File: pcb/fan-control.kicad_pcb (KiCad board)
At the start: 2 copper layers, 30 x 65 mm, 47 parts, among them J1 USB_C_Receptacle_USB2.0_14P, J2 USB_C_Receptacle_USB2.0_14P, Q1 BSS138, SW1 SW_Push, SW2 SW_Push, U1 ESP32-C6-WROOM-1-N8, U2 MPM3610GQV-P

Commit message: some layout
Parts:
- D1, D10, D2, D3, D4, D5, D6, D7, D8, D9: moved to B.Cu
- SW1: footprint Button_Switch_THT:SW_PUSH_6mm -> Footprints:4P-3.4x3.4mm; moved to B.Cu
- SW2: footprint Button_Switch_THT:SW_PUSH_6mm -> Footprints:4P-3.4x3.4mm
- moved R1 80.1 mm to (161.8, 122.0), turned to 180 degrees
- moved R2 79.8 mm to (161.8, 113.1), turned to 180 degrees
- moved R5 77.5 mm to (147.9, 83.2)
- moved R18 76.9 mm to (154.3, 78.2), turned to 90 degrees
- moved R8 75.5 mm to (161.8, 110.6), turned to 180 degrees
- moved C1 73.7 mm to (154.2, 93.8), turned to 90 degrees
- moved R19 73.5 mm to (150.9, 81.7), turned to 90 degrees
- moved R4 70.3 mm to (145.1, 90.4), turned to 90 degrees
- moved R6 69.2 mm to (147.9, 77.3)
- moved R7 68.5 mm to (152.6, 93.8), turned to -90 degrees
- moved R23 67.7 mm to (151.5, 79.1)
- moved R22 67.2 mm to (151.5, 77.4), turned to 180 degrees
- moved R3 67.1 mm to (145.1, 95.9), turned to -90 degrees
- moved R20 63.5 mm to (152.5, 81.7), turned to -90 degrees
- moved C4 63.0 mm to (144.5, 103.5), turned to 90 degrees
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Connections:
- D1 pad 1: /LED1 -> Net-(D1-K)
- D1 pad 2: Net-(D1-A) -> +3V3
- D10 pad 1: /LED10 -> Net-(D10-K)
- D10 pad 2: Net-(D10-A) -> +3V3
- D2 pad 1: /LED2 -> Net-(D2-K)
- D2 pad 2: Net-(D2-A) -> +3V3
- D3 pad 1: /LED3 -> Net-(D3-K)
- D3 pad 2: Net-(D3-A) -> +3V3
- D4 pad 1: /LED4 -> Net-(D4-K)
- D4 pad 2: Net-(D4-A) -> +3V3
- D5 pad 1: /LED5 -> Net-(D5-K)
- D5 pad 2: Net-(D5-A) -> +3V3
- D6 pad 1: /LED6 -> Net-(D6-K)
- D6 pad 2: Net-(D6-A) -> +3V3
- D7 pad 1: /LED7 -> Net-(D7-K)
- D7 pad 2: Net-(D7-A) -> +3V3
- D8 pad 1: /LED8 -> Net-(D8-K)
- D8 pad 2: Net-(D8-A) -> +3V3
- D9 pad 1: /LED9 -> Net-(D9-K)
- D9 pad 2: Net-(D9-A) -> +3V3
- R10 pad 1: +3V3 -> Net-(D3-K)
- R10 pad 2: Net-(D3-A) -> /LED3
- R11 pad 1: +3V3 -> Net-(D4-K)
- R11 pad 2: Net-(D4-A) -> /LED4
- R12 pad 1: +3V3 -> Net-(D5-K)
- R12 pad 2: Net-(D5-A) -> /LED5
- R13 pad 1: +3V3 -> Net-(D6-K)
- R13 pad 2: Net-(D6-A) -> /LED6
- R14 pad 1: +3V3 -> Net-(D7-K)
- R14 pad 2: Net-(D7-A) -> /LED7
- R15 pad 1: +3V3 -> Net-(D8-K)
- R15 pad 2: Net-(D8-A) -> /LED8
- R16 pad 1: +3V3 -> Net-(D9-K)
- R16 pad 2: Net-(D9-A) -> /LED9
- R17 pad 1: +3V3 -> Net-(D10-K)
- R17 pad 2: Net-(D10-A) -> /LED10
- R8 pad 1: +3V3 -> Net-(D1-K)
- R8 pad 2: Net-(D1-A) -> /LED1
- R9 pad 1: +3V3 -> Net-(D2-K)
- R9 pad 2: Net-(D2-A) -> /LED2
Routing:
- net +10V: track 0.00 -> 23.4 mm, vias 0 -> 2
- net +3V3: track 0.00 -> 15.5 mm, vias 0 -> 2
- net /BOOT: track 0.00 -> 7.60 mm
- net /FAN_PWM: track 0.00 -> 6.65 mm
- net /BUTTON: track 0.00 -> 5.25 mm, vias 0 -> 1
- net Net-(J1-CC1): track 0.00 -> 4.47 mm
- net Net-(U2-FB): track 0.00 -> 3.70 mm
- net /LED5: track 0.00 -> 2.56 mm
- net /TACH: track 0.00 -> 2.46 mm
- net /D-: track 0.00 -> 2.44 mm
- net /D+: track 0.00 -> 2.44 mm
- net /LED6: track 0.00 -> 2.42 mm
- net /LED10: track 0.00 -> 2.40 mm
- net /LED3: track 0.00 -> 2.35 mm
- net /LED7: track 0.00 -> 2.29 mm
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
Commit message: Routing
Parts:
- removed J2: USB_C_Receptacle_USB2.0_14P, Connector_USB:USB_C_Receptacle_GCT_USB4105-xx-A_16P_TopMnt_Horizontal
- removed R3, R4: 5.1k, Resistor_SMD:R_0603_1608Metric_Pad0.98x0.95mm_HandSolder
- added J3: Conn_ARM_SWD_TagConnect_TC2030-NL, Connector:Tag-Connect_TC2030-IDC-NL_2x03_P1.27mm_Vertical, F.Cu at (137.6, 85.0)
- moved D3 35.6 mm to (158.8, 121.3)
- moved D4 35.6 mm to (158.8, 115.6)
- moved D1 35.6 mm to (150.0, 127.7)
- moved D10 35.6 mm to (144.6, 125.9)
- moved D2 35.6 mm to (155.4, 125.9)
- moved D5 35.6 mm to (155.4, 111.0)
- moved D6 35.6 mm to (150.0, 109.2)
- moved D7 35.6 mm to (144.6, 111.0)
- moved D8 35.6 mm to (141.2, 115.6)
- moved D9 35.6 mm to (141.2, 121.3)
- moved R1 34.6 mm to (152.7, 88.6), turned to -90 degrees
- moved R2 30.7 mm to (143.3, 88.6), turned to -90 degrees
- moved H1 27.2 mm to (150.0, 118.6)
- moved R16 25.0 mm to (137.4, 89.7)
- moved SW2 22.1 mm to (137.3, 124.1), turned to 90 degrees
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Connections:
- R10 pad 2: /LED3 -> /LED10
- R11 pad 2: /LED4 -> /LED1
- R12 pad 2: /LED5 -> /LED3
- R13 pad 2: /LED6 -> /LED2
- R14 pad 2: /LED7 -> /LED8
- R15 pad 2: /LED8 -> /LED5
- R16 pad 2: /LED9 -> /LED4
- R17 pad 2: /LED10 -> /LED6
- R8 pad 2: /LED1 -> /LED7
- R9 pad 2: /LED2 -> /LED9
- U1 pad 12: /LED1 -> unconnected-(U1-IO11-Pad12)
- U1 pad 13: /D- -> unconnected-(U1-IO12-Pad13)
- U1 pad 14: /D+ -> /LED4
- U1 pad 24: /LED4 -> /RX
- U1 pad 25: /LED3 -> /TX
- U1 pad 26: unconnected-(U1-IO3-Pad26) -> /LED1
- U1 pad 27: unconnected-(U1-IO2-Pad27) -> /LED3
- U1 pad 5: unconnected-(U1-IO5-Pad5) -> /ESP_PWM
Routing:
- net +3V3: track 15.5 -> 128.4 mm, vias 2 -> 4
- net Net-(D9-K): track 0.00 -> 34.7 mm, vias 0 -> 3
- net /RX: track 0.00 -> 30.4 mm, vias 0 -> 2
- net /TX: track 0.00 -> 30.3 mm, vias 0 -> 2
- net Net-(D2-K): track 0.00 -> 17.4 mm, vias 0 -> 1
- net Net-(D1-K): track 0.00 -> 16.9 mm, vias 0 -> 1
- net Net-(D3-K): track 0.00 -> 14.3 mm, vias 0 -> 1
- net Net-(D10-K): track 0.00 -> 13.9 mm, vias 0 -> 1
- net /ESP_PWM: track 2.04 -> 10.3 mm
- net Net-(D8-K): track 0.00 -> 7.42 mm, vias 0 -> 1
- net Net-(D4-K): track 0.00 -> 6.50 mm, vias 0 -> 1
- net /BOOT: track 7.60 -> 14.0 mm
- net +10V: track 23.4 -> 18.6 mm
- net Net-(D7-K): track 0.00 -> 4.68 mm, vias 0 -> 1
- net Net-(D6-K): track 0.00 -> 3.76 mm, vias 0 -> 1
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- added copper zone on B.Cu, net GND
- added copper zone on F.Cu, net GND

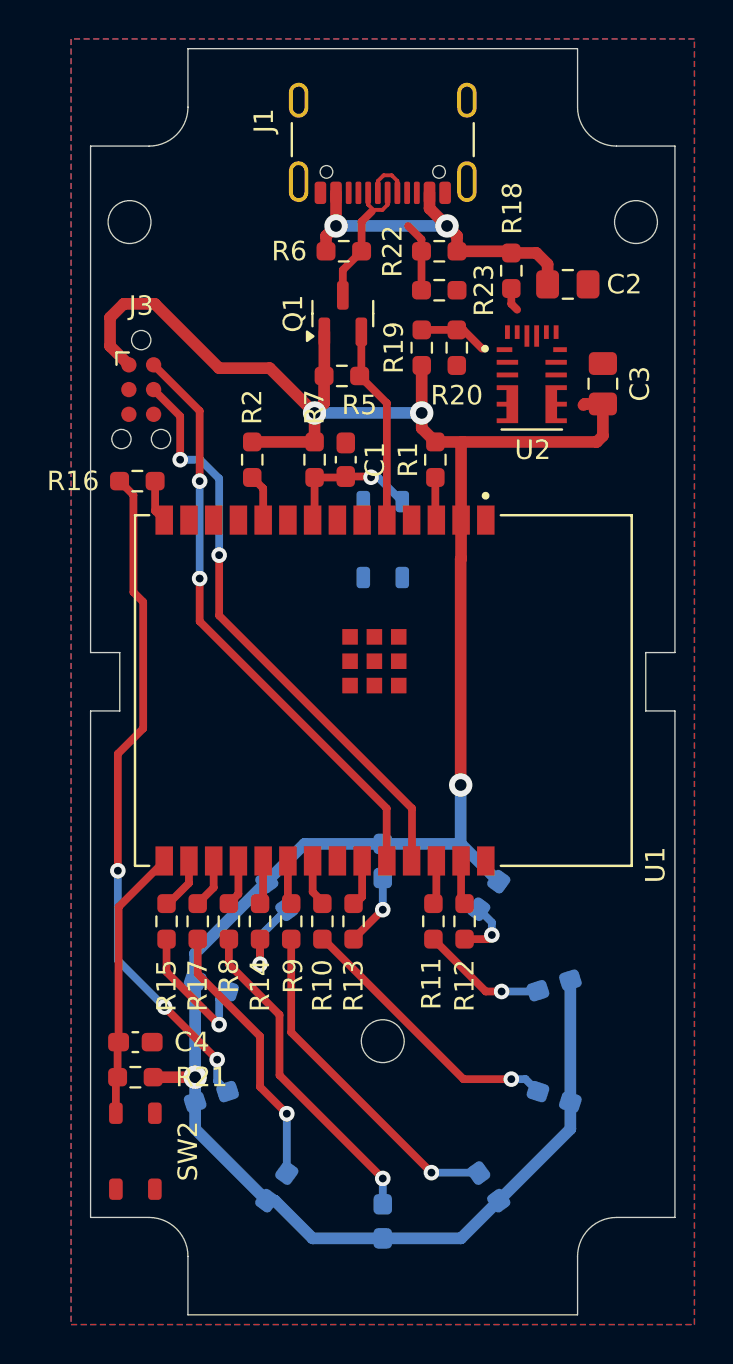
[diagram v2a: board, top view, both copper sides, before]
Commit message: drc, nearing end of layout
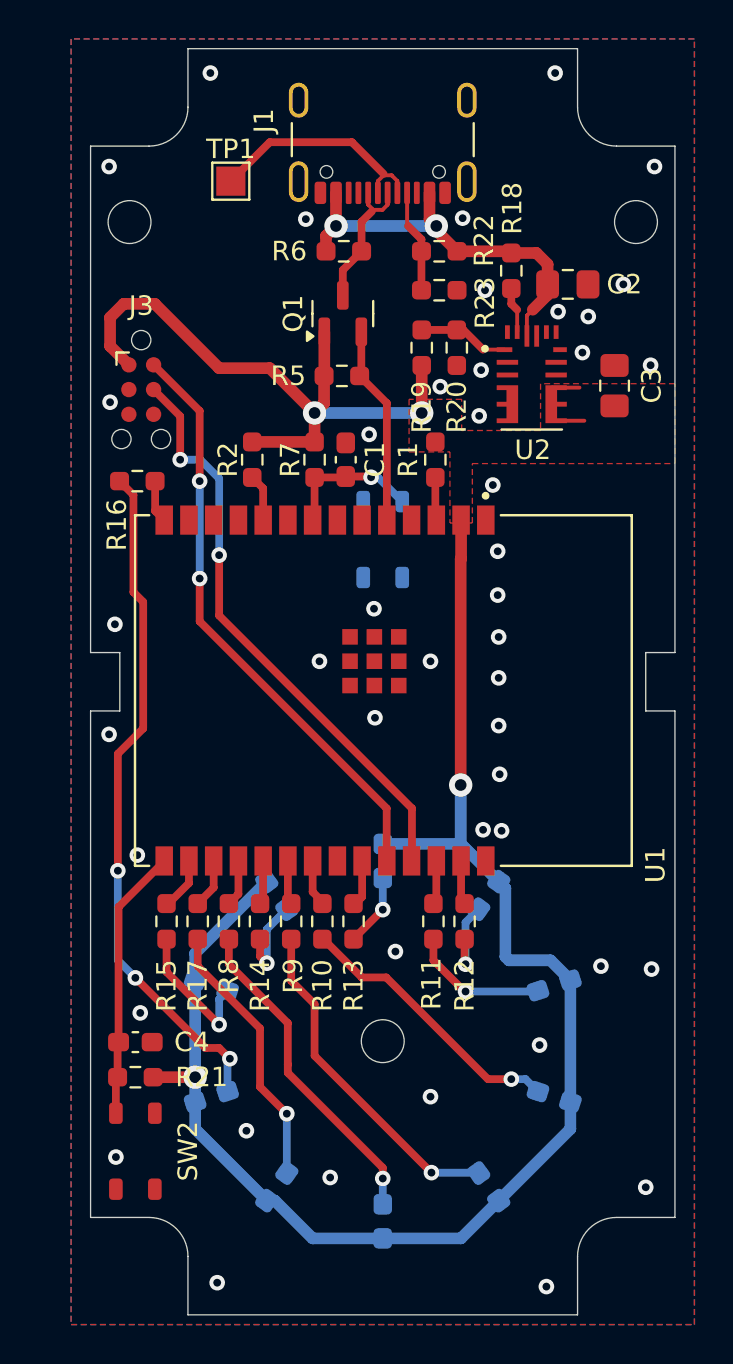
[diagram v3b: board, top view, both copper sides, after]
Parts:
- added TP1: TestPoint, TestPoint:TestPoint_Pad_1.5x1.5mm, F.Cu at (142.2, 74.3)
- moved C3 0.61 mm to (161.9, 84.8)
- moved H1 0.15 mm to (150.0, 118.5)
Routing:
- net +3V3: track 128.4 -> 117.0 mm
- net /TACH: track 2.46 -> 11.8 mm
- net +10V: track 18.6 -> 21.1 mm
- net Net-(J1-CC1): track 3.58 -> 5.31 mm
- net Net-(D5-K): track 3.09 -> 4.41 mm
- net Net-(U2-FB): track 3.50 -> 4.67 mm
- net Net-(U2-EN): track 1.21 -> 2.36 mm
- net Net-(D4-K): track 6.50 -> 7.08 mm
- net Net-(D9-K): track 34.7 -> 35.2 mm
- net GND: vias 0 -> 45
- added copper zone on F.Cu, net +3V3
